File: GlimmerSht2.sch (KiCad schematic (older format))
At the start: 12 parts, among them J3 CONN_02X17, J4 CONN_02X20, J5 CONN_02X17, J6 CONN_02X01, U5 TSOP38238

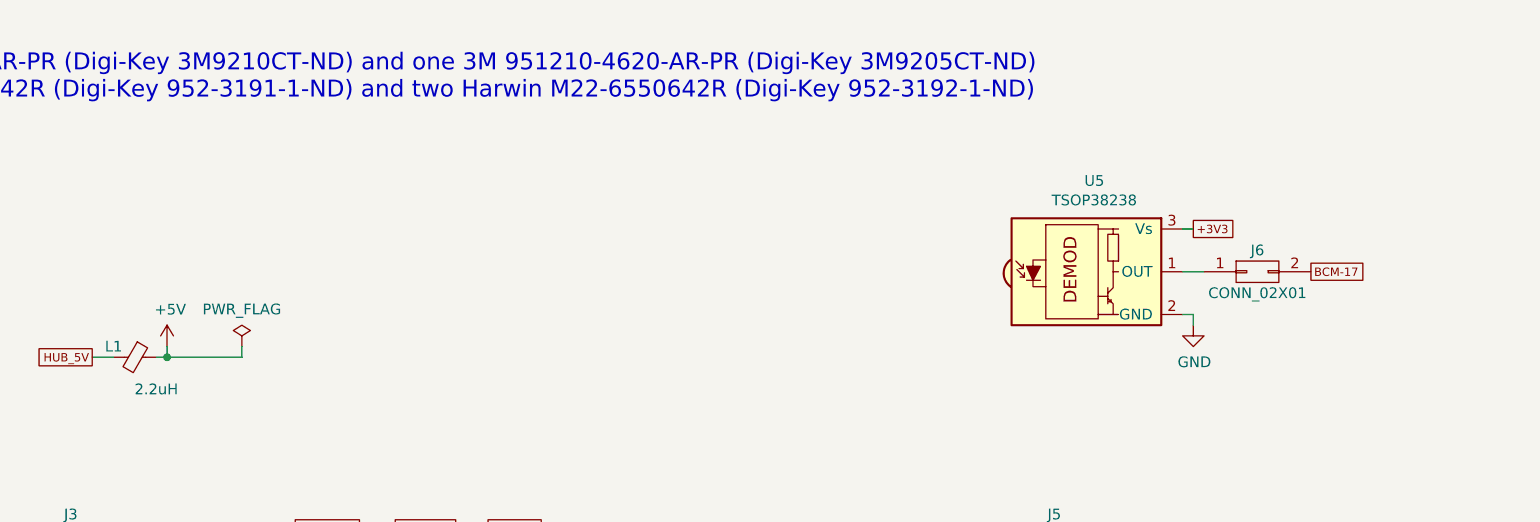
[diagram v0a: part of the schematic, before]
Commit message: Added solder jumper to IR Rcvr; README edits
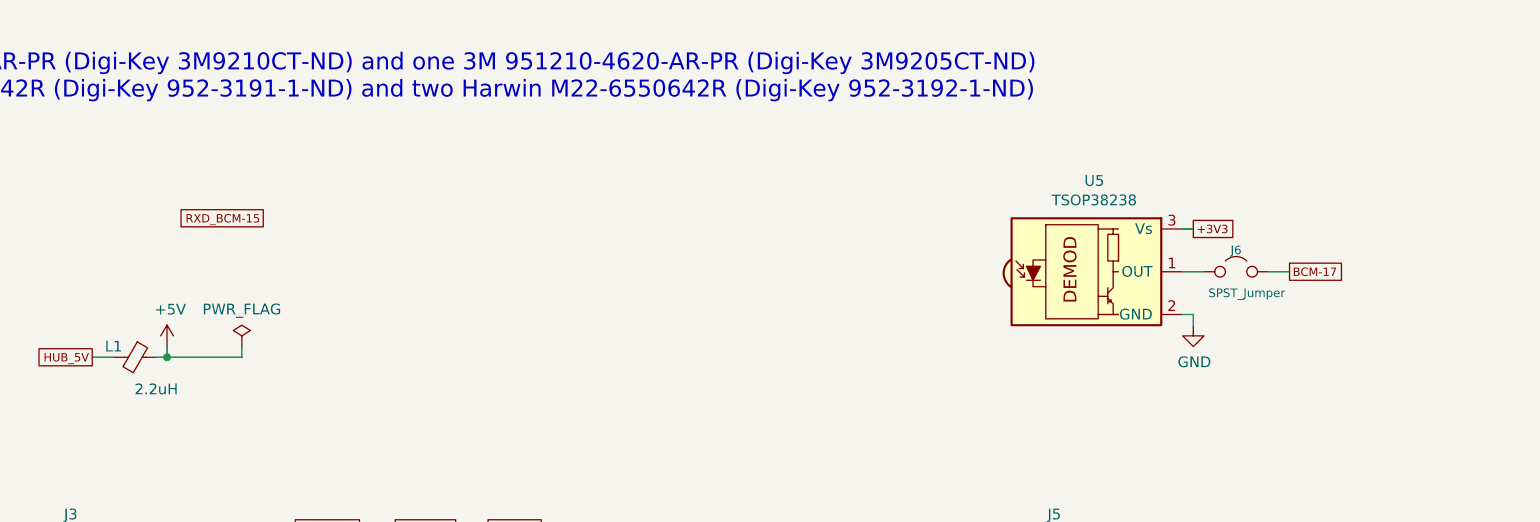
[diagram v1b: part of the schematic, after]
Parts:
- removed J6: CONN_02X01, Pin_Headers:Pin_Header_Straight_2x01_Pitch2.54mm, symbol CONN_02X01
- added J6: SPST_Jumper, SolderJumpers:SPST_Jumper, symbol SPST_Jumper
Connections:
- net BCM-17: now also J6.2 (B)
- net at U5.1 (OUT): now also J6.1 (A)
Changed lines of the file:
@@
 LIBS:dmmt5401
 LIBS:7215
+LIBS:SolderJumpers
 LIBS:pi-top_Glimmer-cache
 EELAYER 26 0
@@
 Text GLabel 8600 1650 2    39   UnSpc ~ 0
 +3V3
-$Comp
-L CONN_02X01 J6
-U 1 1 59249527
-P 8900 1850
-F 0 "J6" H 8900 1950 50  0000 C CNN
-F 1 "CONN_02X01" H 8900 1750 50  0000 C CNN
-F 2 "Pin_Headers:Pin_Header_Straight_2x01_Pitch2.54mm" H 8900 650 50  0001 C CNN
-F 3 "" H 8900 650 50  0001 C CNN
-	1    8900 1850
-	1    0    0    -1
-$EndComp
-Text GLabel 9150 1850 2    39   UnSpc ~ 0
+Text GLabel 9050 1850 2    39   UnSpc ~ 0
 BCM-17
 Wire Wire Line
@@
 	2300 3350 2300 3450
 Connection ~ 2300 3400
+Text GLabel 4250 1600 0    39   UnSpc ~ 0
+RXD_BCM-15
+$Comp
+L SPST_Jumper J6
+U 1 1 59516DEC
+P 8800 1850
+F 0 "J6" H 8800 1950 40  0000 C CNN
+F 1 "SPST_Jumper" H 8850 1750 40  0000 C CNN
+F 2 "SolderJumpers:SPST_Jumper" H 8800 1850 60  0001 C CNN
+F 3 "" H 8800 1850 60  0001 C CNN
+	1    8800 1850
+	1    0    0    -1
+$EndComp
+Wire Wire Line
+	9050 1850 8950 1850
 $EndSCHEMATC

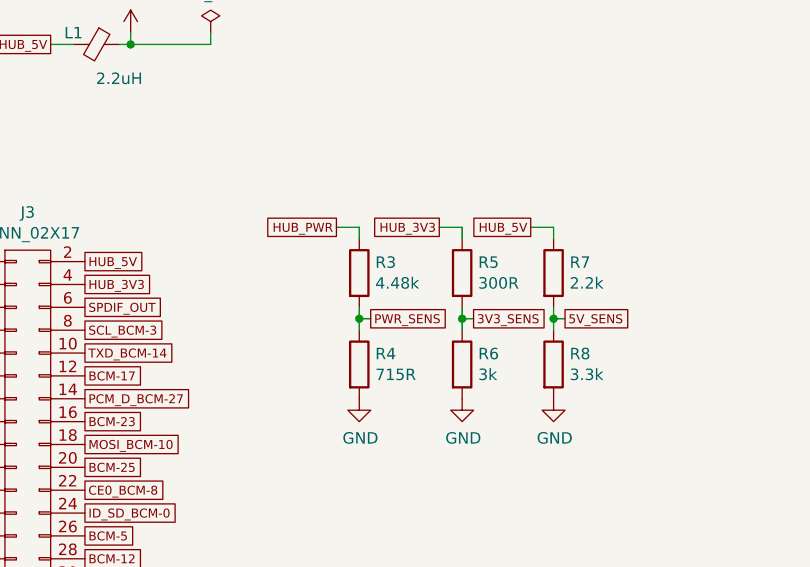
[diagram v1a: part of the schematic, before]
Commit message: Adding BOM
Parts availability caused change to schem2
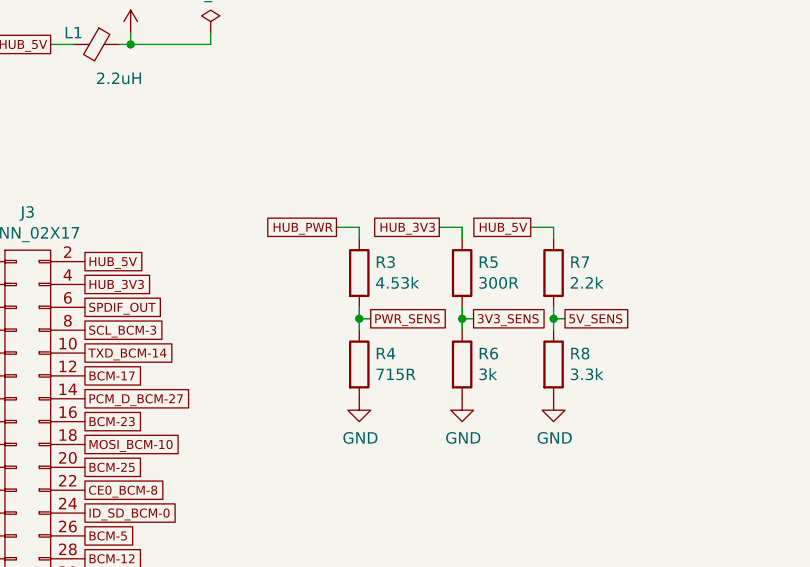
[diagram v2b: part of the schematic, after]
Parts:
- R3: value 4.48k -> 4.53k
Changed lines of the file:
@@
 P 4800 3250
 F 0 "R3" H 4870 3296 50  0000 L CNN
-F 1 "4.48k" H 4870 3205 50  0000 L CNN
+F 1 "4.53k" H 4870 3205 50  0000 L CNN
 F 2 "Resistors_SMD:R_0805_HandSoldering" V 4730 3250 50  0001 C CNN
 F 3 "" H 4800 3250 50  0001 C CNN
